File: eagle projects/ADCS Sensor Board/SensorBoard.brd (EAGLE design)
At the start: 91 x 91 mm, 103 parts, among them J1 HDR_10_EZFET_DEBUGGER, J2 MTI-1_8428-11B1-RK-TP, J3 HDR_2X5_GRPB052VWQS-RC, Q1 PMV16XN, Q2 IRLML6246TRPBF, Q3 IRLML2246TRPBF, U1 MSP430F5529IPN, U2 LMV321, U3 ADS7841E_2K5, U4 LMV321, U5 LMV321, Y1 32.768kHz, Y2 CSTCR4M00G15L99

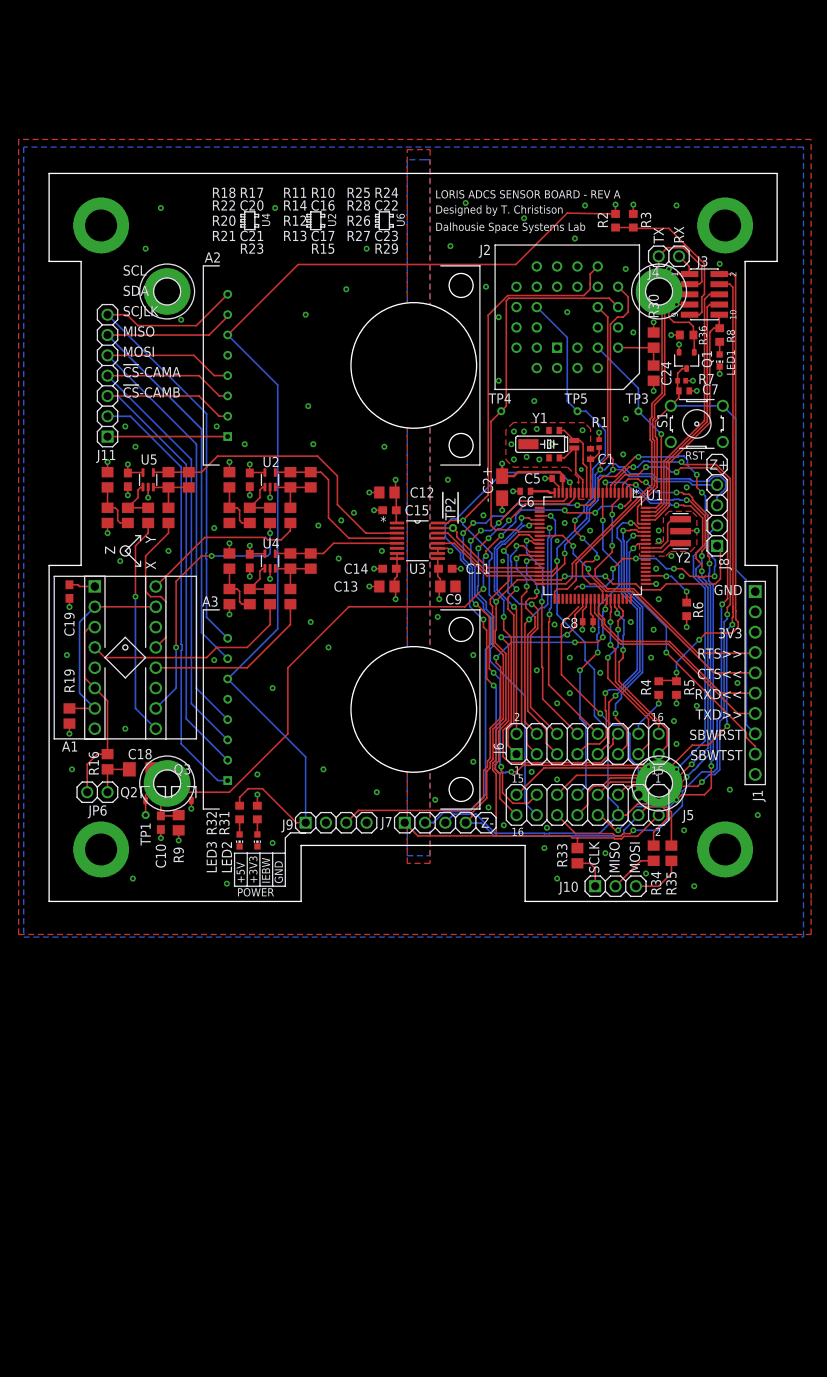
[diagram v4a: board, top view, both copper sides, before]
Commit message: Added BNO055 IMU to sensor board schematic
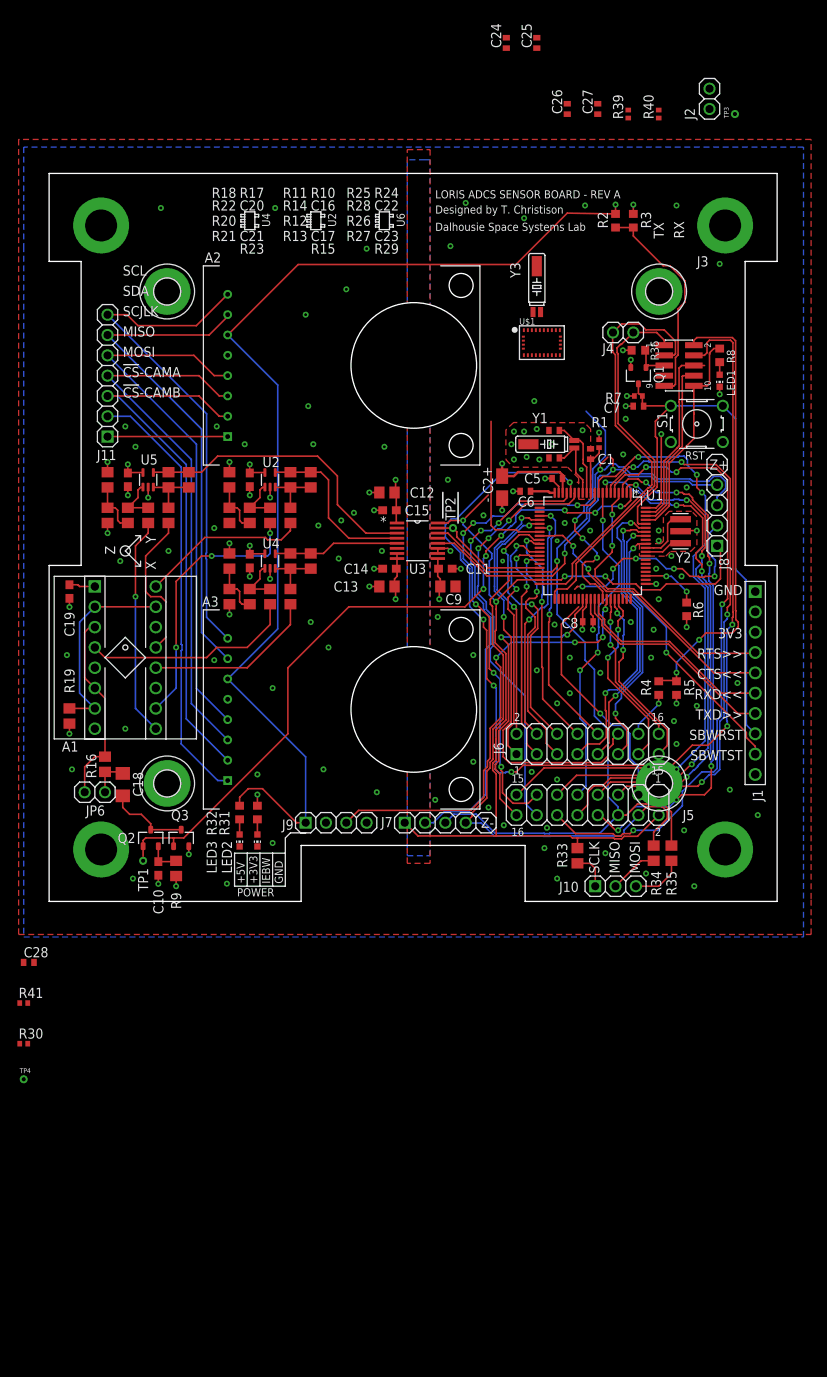
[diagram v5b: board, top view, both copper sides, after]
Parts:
- removed DRILEGEND: (no value), drilegend:DRILEGEND
- removed TP5: TESTPOINT, my_library:TP_P76H50
- added C25, C28: 0.1u, rcl:C0402
- added C26, C27: 22p, rcl:C0402
- added R39, R40, R41: 10k, rcl:R0402
- added U$1: (no value), my_library:BNO055
- added Y3: 32.768kHz, my_library:MS3V-T1R
- C24: value 470n -> 1u; device rcl:C0805 -> rcl:C0402
- J2: value MTI-1_8428-11B1-RK-TP -> (none); device my_library:PLCC-28_SOCKET_TH -> my_library:1X02
- R30: value 27R -> 10k; device rcl:R0805 -> rcl:R0402
- U2, U4, U5: device my_library:SOT23-5P65_210X110L36X22N -> my_library:SC70-5P65_210X110L36X22N
- moved R30 118.0 mm to (-3.17, -17.8), turned to 0 degrees
- moved TP4 102.6 mm to (-3.17, -22.2)
- moved C24 45.2 mm to (57.1, 107.3)
- moved TP3 39.1 mm to (85.7, 98.4)
- moved J2 36.5 mm to (82.5, 100.3), turned to 90 degrees
- moved J4 11.1 mm to (71.8, 71.1)
- moved J3 9.44 mm to (78.7, 67.0)
- moved Q1 6.33 mm to (73.7, 65.7)
- moved R36 6.33 mm to (73.7, 68.9)
- moved C7 6.02 mm to (73.7, 61.9), turned to 180 degrees
- moved R7 5.72 mm to (73.7, 63.2), turned to 180 degrees
- moved Q2 5.72 mm to (12.7, 7.94)
- moved Q3 5.72 mm to (16.5, 7.94)
- moved TP1 5.72 mm to (11.7, 5.08)
- moved C10 5.72 mm to (13.7, 4.13)
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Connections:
- new net BNO055_INT: TP4.1, U$1.14
- new net BNO055_RST: R41.1, TP3.1, U$1.11
- new net N$13: C24.2, U$1.9
- new net N$14: C26.2, U$1.27, Y3.P2
- new net N$15: C27.2, U$1.26, Y3.P1
- new net N$16: J2.1, U$1.7
- new net N$17: J2.2, U$1.8
- net !CS!_MTI: no longer J2.9, TP4.1
- net !RST!_MTI: no longer J2.6, TP3.1
- net +3V3: now also C25.2, C28.2, R30.2, R39.2, R40.2, R41.2, U$1.28, U$1.3; no longer J2.15, J2.7, R30.1
- net GND: now also C25.1, C26.1, C27.1, C28.1, U$1.10, U$1.15, U$1.16, U$1.17, U$1.18, U$1.2, U$1.25, U$1.5, U$1.6, Y3.P3; no longer J2.13, J2.25, J2.4, J2.8
- net MTI_DRDY: no longer J2.22, TP5.1
- net N$7: now also R30.1, U$1.4; no longer C24.2, J2.5, R30.2
- net UCB0_SPI_CLK: no longer J2.12
- net UCB0_SPI_MISO: no longer J2.11
- net UCB0_SPI_MOSI: no longer J2.10
- net UCB1_I2C_SCL: now also R40.1, U$1.19
- net UCB1_I2C_SDA: now also R39.1, U$1.20
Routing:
- net UCB0_SPI_CLK: track 160.5 -> 120.7 mm
- net !CS!_MTI: track 49.8 -> 19.4 mm
- net UCB0_SPI_MISO: track 138.9 -> 115.8 mm
- net UCB0_SPI_MOSI: track 144.4 -> 125.1 mm
- net MTI_DRDY: track 46.1 -> 29.9 mm
- net !RST!_MTI: track 24.9 -> 10.8 mm
- net RESERVED_2: track 31.6 -> 21.5 mm
- net RESERVED_1: track 32.4 -> 23.8 mm
- net MSP_OBC_RESET: track 11.9 -> 4.61 mm
- net N$7: track 6.67 -> 0.00 mm
- net UCA0TXD: track 60.0 -> 53.5 mm
- net SEN_BRD_5V_PRESENT: track 20.9 -> 26.9 mm
- net UCA0RXD: track 52.5 -> 47.0 mm
- net N$9: track 5.97 -> 10.3 mm
- net ACT_BRD_5V_SHIFTED: track 60.3 -> 56.2 mm
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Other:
- board text removed: "01-16"
- board text removed: "01-20"
- board text removed: "LAYER-STACK"

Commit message: Schematic Updates
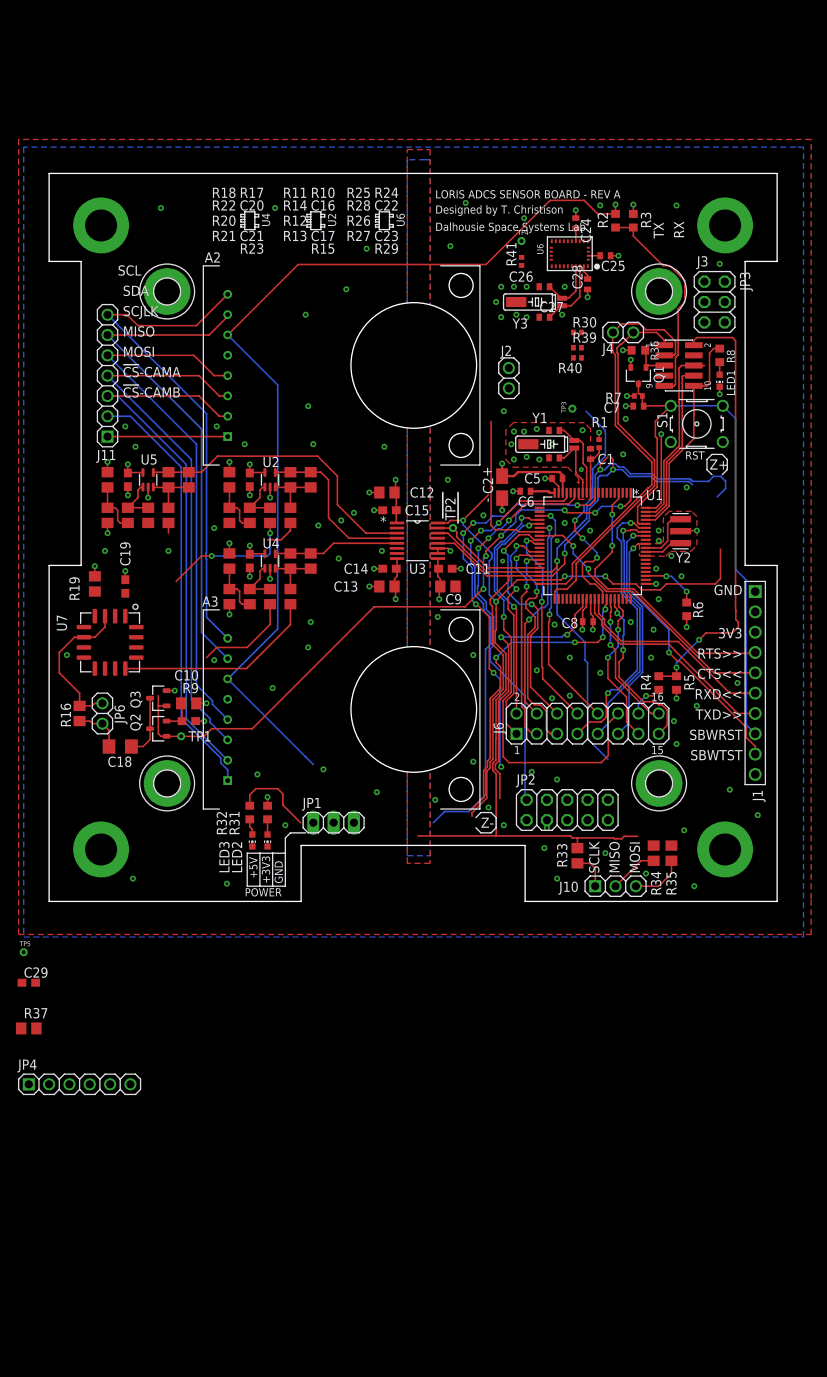
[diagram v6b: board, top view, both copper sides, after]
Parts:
- removed A1: HMC1053PA0242, my_library:PA0242
- removed J5: (no value), my_library:2X08
- removed J7, J8, J9: (no value), my_library:1X04
- removed U$1: (no value), my_library:BNO055
- added C29: 0.1u, rcl:C0603
- added JP1: (no value), pinhead:1X03
- added JP2: (no value), pinhead:2X05
- added JP3: (no value), pinhead:2X03
- added JP4: (no value), my_library:1X06
- added R37: 10k, rcl:R0805
- added TP5: TESTPOINT, my_library:TP_P76H50
- added U6: (no value), my_library:BNO055
- added U7: HMC1053, my_library:LCCS16P127_736X736X279L127X50N
- C10: value 0.1u -> 1u
- C18: value 1n -> 0.1u
- moved TP4 121.9 mm to (59.1, 82.5)
- moved R30 112.7 mm to (66.0, 71.1)
- moved R41 111.7 mm to (59.1, 80.0), turned to 90 degrees
- moved C28 109.8 mm to (67.3, 77.2), turned to 90 degrees
- moved J2 43.0 mm to (57.5, 65.4), turned to 270 degrees
- moved TP3 42.1 mm to (65.4, 61.6)
- moved R40 32.1 mm to (66.0, 67.9), turned to 180 degrees
- moved R39 29.9 mm to (66.0, 69.2), turned to 0 degrees
- moved C25 27.9 mm to (69.5, 80.7), turned to 180 degrees
- moved C27 26.9 mm to (61.9, 73.0), turned to 0 degrees
- moved C24 24.2 mm to (65.8, 84.8), turned to 270 degrees
- moved C26 22.4 mm to (61.9, 76.8), turned to 0 degrees
- moved R9 20.7 mm to (17.5, 24.8), turned to 0 degrees
- moved C10 18.8 mm to (17.5, 22.5), turned to 180 degrees
- moved Q3 17.7 mm to (13.7, 25.4), turned to 90 degrees
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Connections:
- removed net !COUNT_EN: J5.5, U1.6
- removed net !CS!_SPEED_X: J5.8, U1.3
- removed net !CS!_SPEED_Y: J5.10, U1.2
- removed net !CS!_SPEED_Z: J5.12, U1.5
- removed net !LOAD_SPEED: J5.9, U1.8
- removed net !SPEED_CLR: J5.7, U1.7
- new net N$18: JP2.8
- new net N$19: JP2.10
- new net N$29: TP5.1, U3.2
- new net N$31: C29.1, R37.2, U3.7
- net !CS!_CURRENT_SENSE_1: now also JP3.1; no longer J5.11
- net !CS!_CURRENT_SENSE_2: now also JP3.3; no longer J5.13
- net !CS!_SUN_X+: now also JP2.2; no longer J5.16
- net !CS!_SUN_X-: now also JP2.7; no longer J5.14
- net !CS!_SUN_Y+: now also JP2.4; no longer J5.3
- net !CS!_SUN_Y-: now also JP2.9; no longer J5.1
- net !CS!_SUN_Z+: now also JP4.5; no longer J8.2
- net !CS!_SUN_Z-: now also JP2.6; no longer J7.2
- net +3V3: now also JP1.2, JP4.1, R37.1, U6.28, U6.3, U7.1; no longer A1.1, J9.2, U$1.28, U$1.3, U3.7
- net +5V: now also JP1.1; no longer J9.1
- net ACT_BRD_3V_PRESENT: now also JP3.5; no longer J5.15
- net BNO055_INT: now also U6.14; no longer U$1.14
- net BNO055_RST: now also U6.11; no longer U$1.11
- net GND: now also C29.2, JP1.3, JP4.6, U6.10, U6.15, U6.16, U6.17, U6.18, U6.2, U6.25, U6.5, U6.6, U7.11, U7.14, U7.5, U7.8; no longer A1.11, A1.14, A1.5, A1.8, J9.4, U$1.10, U$1.15, U$1.16, U$1.17, U$1.18, U$1.2, U$1.25, U$1.5, U$1.6
- net INIT_EPS_BURN_WIRE: no longer J9.3
- net N$13: now also U6.9; no longer U$1.9
- net N$14: now also U6.27, Y3.P1; no longer U$1.27, Y3.P2
- net N$15: now also U6.26, Y3.P2; no longer U$1.26, Y3.P1
- net N$16: now also U6.7; no longer U$1.7
- net N$17: now also U6.8; no longer U$1.8
- net N$36: now also U7.15, U7.2, U7.7; no longer A1.15, A1.2, A1.7
- net N$37: now also U7.3, U7.6; no longer A1.3, A1.6
- net N$7: now also U6.4; no longer U$1.4
- net OUT_A_N: now also U7.10; no longer A1.10
- net OUT_A_P: now also U7.16; no longer A1.16
- net OUT_B_N: now also U7.4; no longer A1.4
- net OUT_B_P: now also U7.12; no longer A1.12
- net OUT_C_N: now also U7.9; no longer A1.9
- net OUT_C_P: now also U7.13; no longer A1.13
- net UCB0_SPI_CLK: now also JP2.5, JP3.2, JP4.4; no longer J5.2, J7.1, J8.1
- net UCB0_SPI_MISO: now also JP2.1, JP3.4, JP4.2; no longer J5.4, J7.4, J8.4
- net UCB0_SPI_MOSI: now also JP2.3, JP3.6, JP4.3; no longer J5.6, J7.3, J8.3
- net UCB1_I2C_SCL: now also U6.19; no longer U$1.19
- net UCB1_I2C_SDA: now also U6.20; no longer U$1.20
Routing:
- net ACT_BRD_3V_PRESENT: track 85.4 -> 0.00 mm, vias 2 -> 0
- net !CS!_SPEED_Z: track 79.4 -> 0.00 mm, vias 4 -> 0
- net !CS!_SUN_Y-: track 77.6 -> 0.00 mm, vias 5 -> 0
- net !CS!_CURRENT_SENSE_1: track 72.7 -> 0.00 mm, vias 4 -> 0
- net !COUNT_EN: track 69.0 -> 0.00 mm, vias 4 -> 0
- net !CS!_SPEED_X: track 66.3 -> 0.00 mm, vias 6 -> 0
- net !CS!_SPEED_Y: track 63.1 -> 0.00 mm, vias 4 -> 0
- net !SPEED_CLR: track 62.2 -> 0.00 mm, vias 4 -> 0
- net UCB0_SPI_MOSI: track 125.1 -> 80.7 mm
- net !LOAD_SPEED: track 41.4 -> 0.00 mm, vias 3 -> 0
- net UCB0_SPI_MISO: track 115.8 -> 78.7 mm
- net !CS!_SUN_Y+: track 29.1 -> 0.00 mm, vias 1 -> 0
- net !CS!_SUN_Z+: track 28.0 -> 0.00 mm, vias 5 -> 0
- net OUT_C_N: track 27.4 -> 0.00 mm, vias 1 -> 0
- net N$36: track 25.1 -> 0.46 mm
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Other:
- board text removed: "IEBW"
